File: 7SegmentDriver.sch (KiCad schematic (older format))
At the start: 8 parts

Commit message: Umsortiert
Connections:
- net BrightnessRegulation renamed BrightnessPWM
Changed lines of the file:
@@
 $Descr A4 11693 8268
 encoding utf-8
-Sheet 9 9
+Sheet 8 9
 Title ""
 Date ""
@@
 $EndComp
 Text HLabel 1400 1350 0    50   Input ~ 0
-BrightnessRegulation
+BrightnessPWM
 Wire Wire Line
 	1400 1850 5150 1850
@@
 U 1 1 6202C821
 P 800 5700
+AR Path="/60D33366/6202C821" Ref="#PWR?"  Part="1"
+AR Path="/60F87146/6202C821" Ref="#PWR?"  Part="1"
 F 0 "#PWR?" H 800 5450 50  0001 C CNN
 F 1 "GND" H 805 5527 50  0000 C CNN
@@
 U 1 1 6202C82F
 P 800 5350
+AR Path="/60D33366/6202C82F" Ref="C?"  Part="1"
+AR Path="/60F87146/6202C82F" Ref="C?"  Part="1"
 F 0 "C?" V 1050 5300 50  0000 L CNN
 F 1 "100n/10V/X7R" V 950 5100 50  0000 L CNN
@@
 U 1 1 620341F4
 P 4500 1100
+AR Path="/60D33366/620341F4" Ref="C?"  Part="1"
+AR Path="/60F87146/620341F4" Ref="C?"  Part="1"
 F 0 "C?" V 4750 1050 50  0000 L CNN
 F 1 "100n/10V/X7R" V 4650 850 50  0000 L CNN

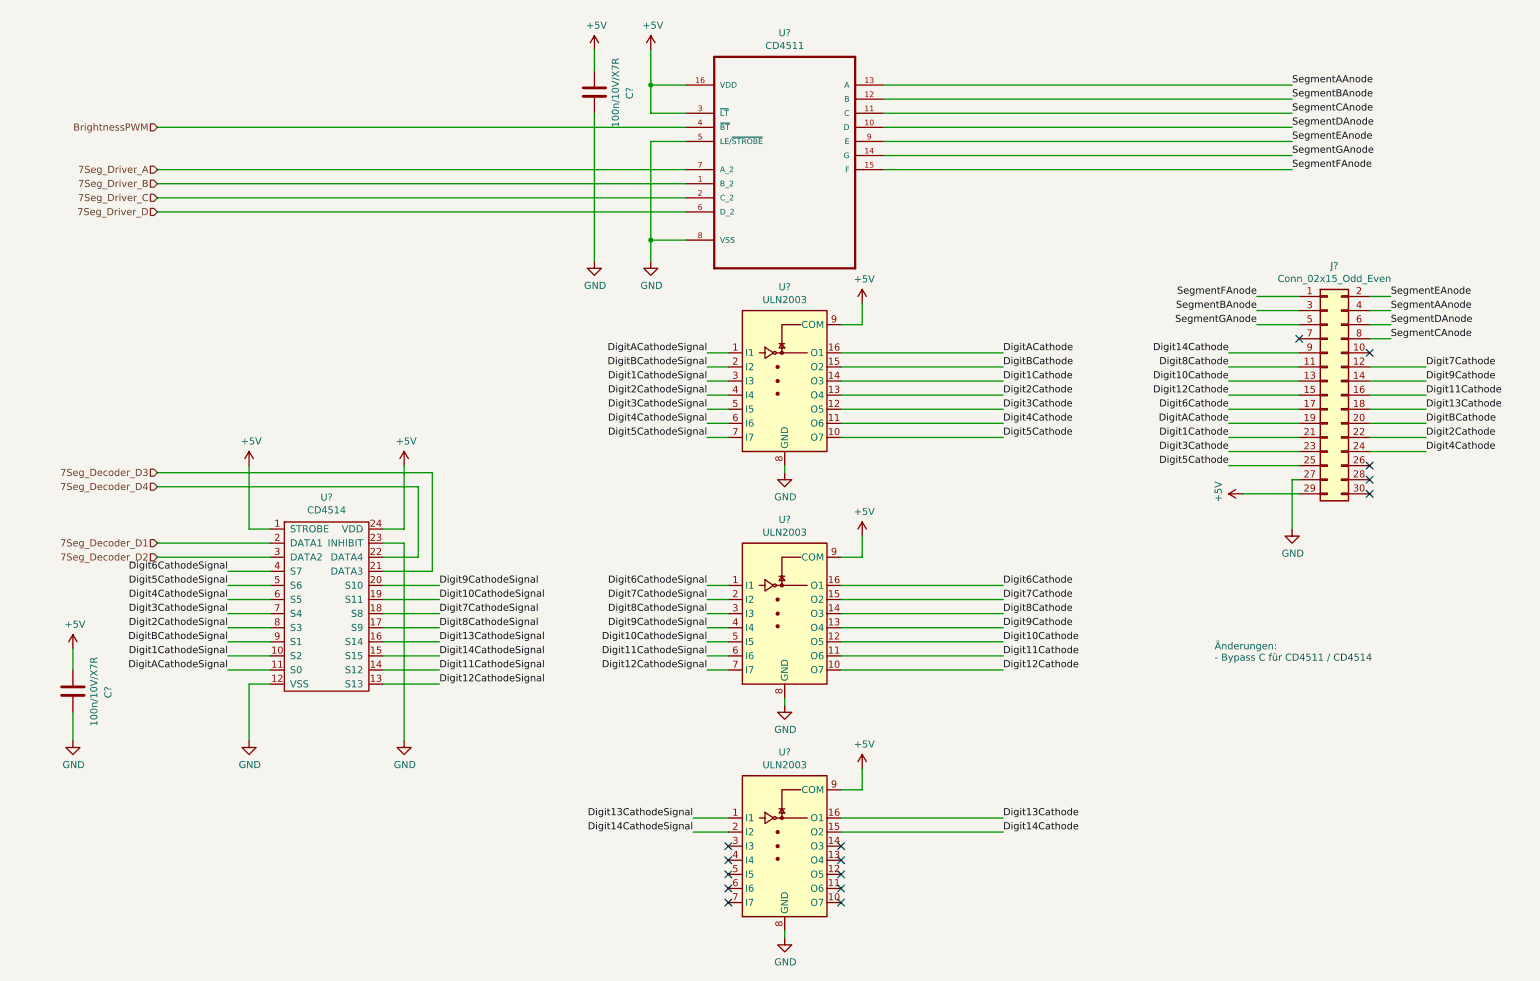
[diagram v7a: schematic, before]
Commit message: [modified:] uln2003 package swap [modified:] Display nomenclature update
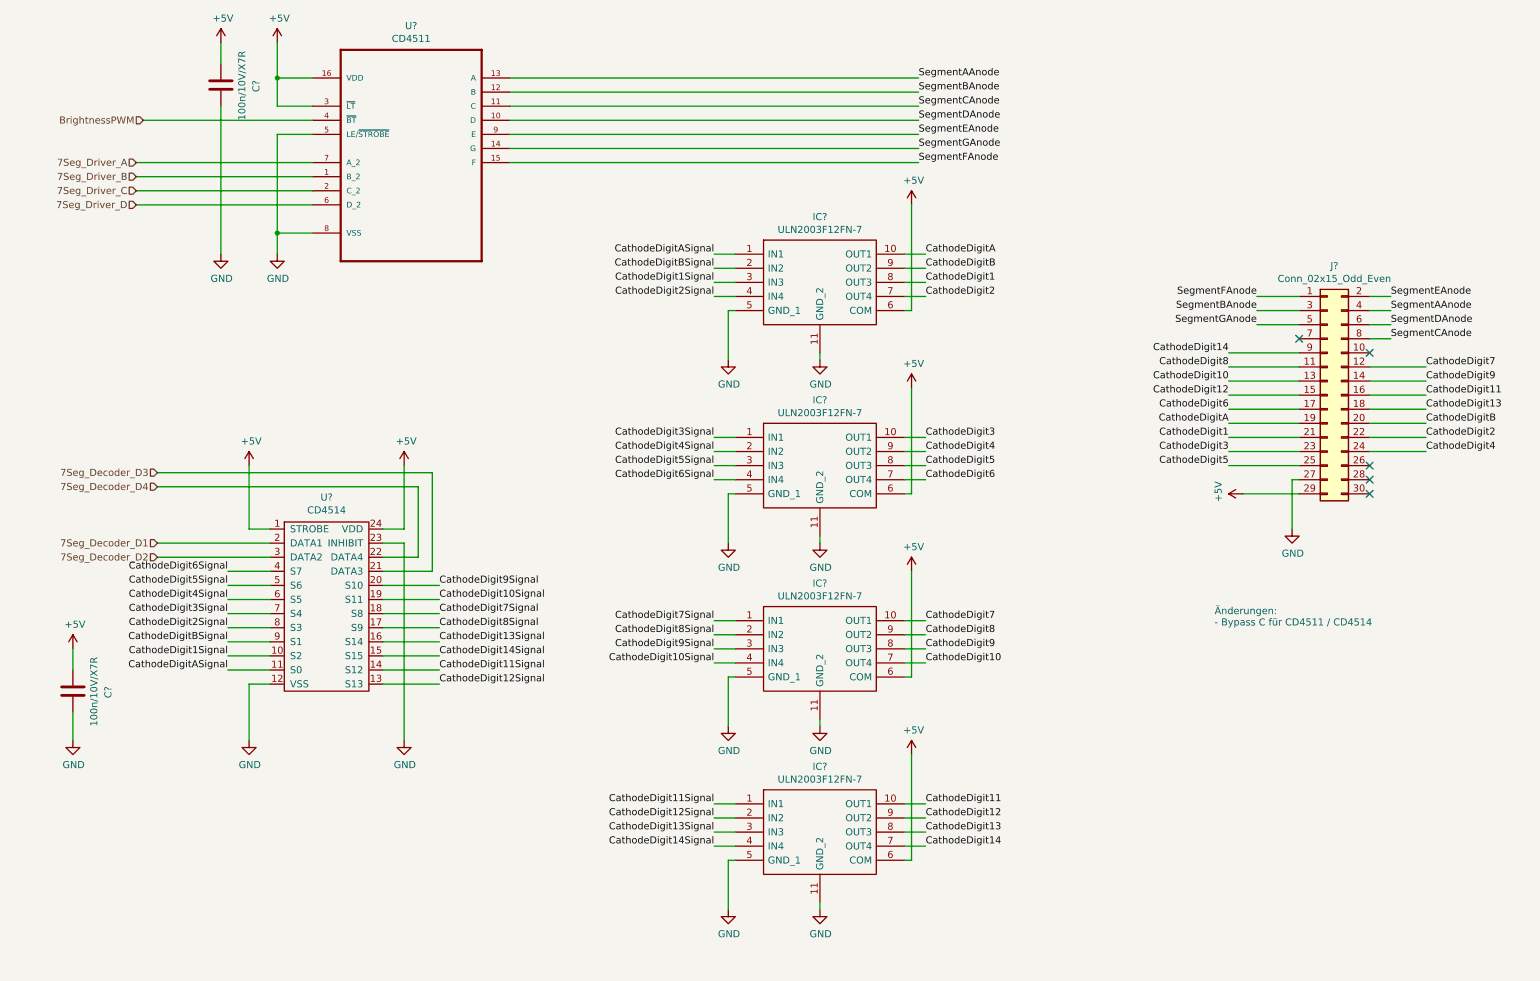
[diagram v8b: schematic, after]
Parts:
- removed U? (x3): ULN2003, symbol Transistor_Array:ULN2003
- added IC? (x4): ULN2003F12FN-7, SON50P300X300X63-11N, symbol TeKaDe:ULN2003F12FN-7
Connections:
- net +5V: now also IC?.6 (COM), IC?.6 (COM), IC?.6 (COM), IC?.6 (COM)
- net GND: now also IC?.11 (GND_2), IC?.11 (GND_2), IC?.11 (GND_2), IC?.11 (GND_2), IC?.5 (GND_1), IC?.5 (GND_1), IC?.5 (GND_1), IC?.5 (GND_1)
- net Digit10Cathode renamed CathodeDigit10
- net CathodeDigit10: now also IC?.7 (OUT4)
- net Digit10CathodeSignal renamed CathodeDigit10Signal
- net CathodeDigit10Signal: now also IC?.4 (IN4)
- net Digit11Cathode renamed CathodeDigit11
- net CathodeDigit11: now also IC?.10 (OUT1)
- net Digit11CathodeSignal renamed CathodeDigit11Signal
- net CathodeDigit11Signal: now also IC?.1 (IN1)
- net Digit12Cathode renamed CathodeDigit12
- net CathodeDigit12: now also IC?.9 (OUT2)
- net Digit12CathodeSignal renamed CathodeDigit12Signal
- net CathodeDigit12Signal: now also IC?.2 (IN2)
- net Digit13Cathode renamed CathodeDigit13
- net CathodeDigit13: now also IC?.8 (OUT3)
- net Digit13CathodeSignal renamed CathodeDigit13Signal
- net CathodeDigit13Signal: now also IC?.3 (IN3)
- net Digit14Cathode renamed CathodeDigit14
- net CathodeDigit14: now also IC?.7 (OUT4)
- net Digit14CathodeSignal renamed CathodeDigit14Signal
- net CathodeDigit14Signal: now also IC?.4 (IN4)
- net Digit1Cathode renamed CathodeDigit1
- net CathodeDigit1: now also IC?.8 (OUT3)
- net Digit1CathodeSignal renamed CathodeDigit1Signal
- net CathodeDigit1Signal: now also IC?.3 (IN3)
- net Digit2Cathode renamed CathodeDigit2
- net CathodeDigit2: now also IC?.7 (OUT4)
- net Digit2CathodeSignal renamed CathodeDigit2Signal
- net CathodeDigit2Signal: now also IC?.4 (IN4)
- net Digit3Cathode renamed CathodeDigit3
- net CathodeDigit3: now also IC?.10 (OUT1)
- net Digit3CathodeSignal renamed CathodeDigit3Signal
- net CathodeDigit3Signal: now also IC?.1 (IN1)
- net Digit4Cathode renamed CathodeDigit4
- net CathodeDigit4: now also IC?.9 (OUT2)
- net Digit4CathodeSignal renamed CathodeDigit4Signal
- net CathodeDigit4Signal: now also IC?.2 (IN2)
- net Digit5Cathode renamed CathodeDigit5
- net CathodeDigit5: now also IC?.8 (OUT3)
- net Digit5CathodeSignal renamed CathodeDigit5Signal
- net CathodeDigit5Signal: now also IC?.3 (IN3)
- net Digit6Cathode renamed CathodeDigit6
- net CathodeDigit6: now also IC?.7 (OUT4)
- net Digit6CathodeSignal renamed CathodeDigit6Signal
- net CathodeDigit6Signal: now also IC?.4 (IN4)
- net Digit7Cathode renamed CathodeDigit7
- net CathodeDigit7: now also IC?.10 (OUT1)
- net Digit7CathodeSignal renamed CathodeDigit7Signal
- net CathodeDigit7Signal: now also IC?.1 (IN1)
- net Digit8Cathode renamed CathodeDigit8
- net CathodeDigit8: now also IC?.9 (OUT2)
- net Digit8CathodeSignal renamed CathodeDigit8Signal
- net CathodeDigit8Signal: now also IC?.2 (IN2)
- net Digit9Cathode renamed CathodeDigit9
- net CathodeDigit9: now also IC?.8 (OUT3)
- net Digit9CathodeSignal renamed CathodeDigit9Signal
- net CathodeDigit9Signal: now also IC?.3 (IN3)
- net DigitACathode renamed CathodeDigitA
- net CathodeDigitA: now also IC?.10 (OUT1)
- net DigitACathodeSignal renamed CathodeDigitASignal
- net CathodeDigitASignal: now also IC?.1 (IN1)
- net DigitBCathode renamed CathodeDigitB
- net CathodeDigitB: now also IC?.9 (OUT2)
- net DigitBCathodeSignal renamed CathodeDigitBSignal
- net CathodeDigitBSignal: now also IC?.2 (IN2)
- no-connect marks 15 -> 5
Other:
- moved on the sheet: C?, U?
